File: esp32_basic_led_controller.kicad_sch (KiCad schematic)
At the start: 16 parts, among them J1 Barrel_Jack_Switch_Pin3Ring, J2 Conn_01x03, J3 Screw_Terminal_01x02, Q1 IRF8721PBF-1, SW1 SW_DIP_x01, U1 ESP32-WROOM-32U, U2 LD1117S33TR_SOT223, U3 I2C_SENS_1

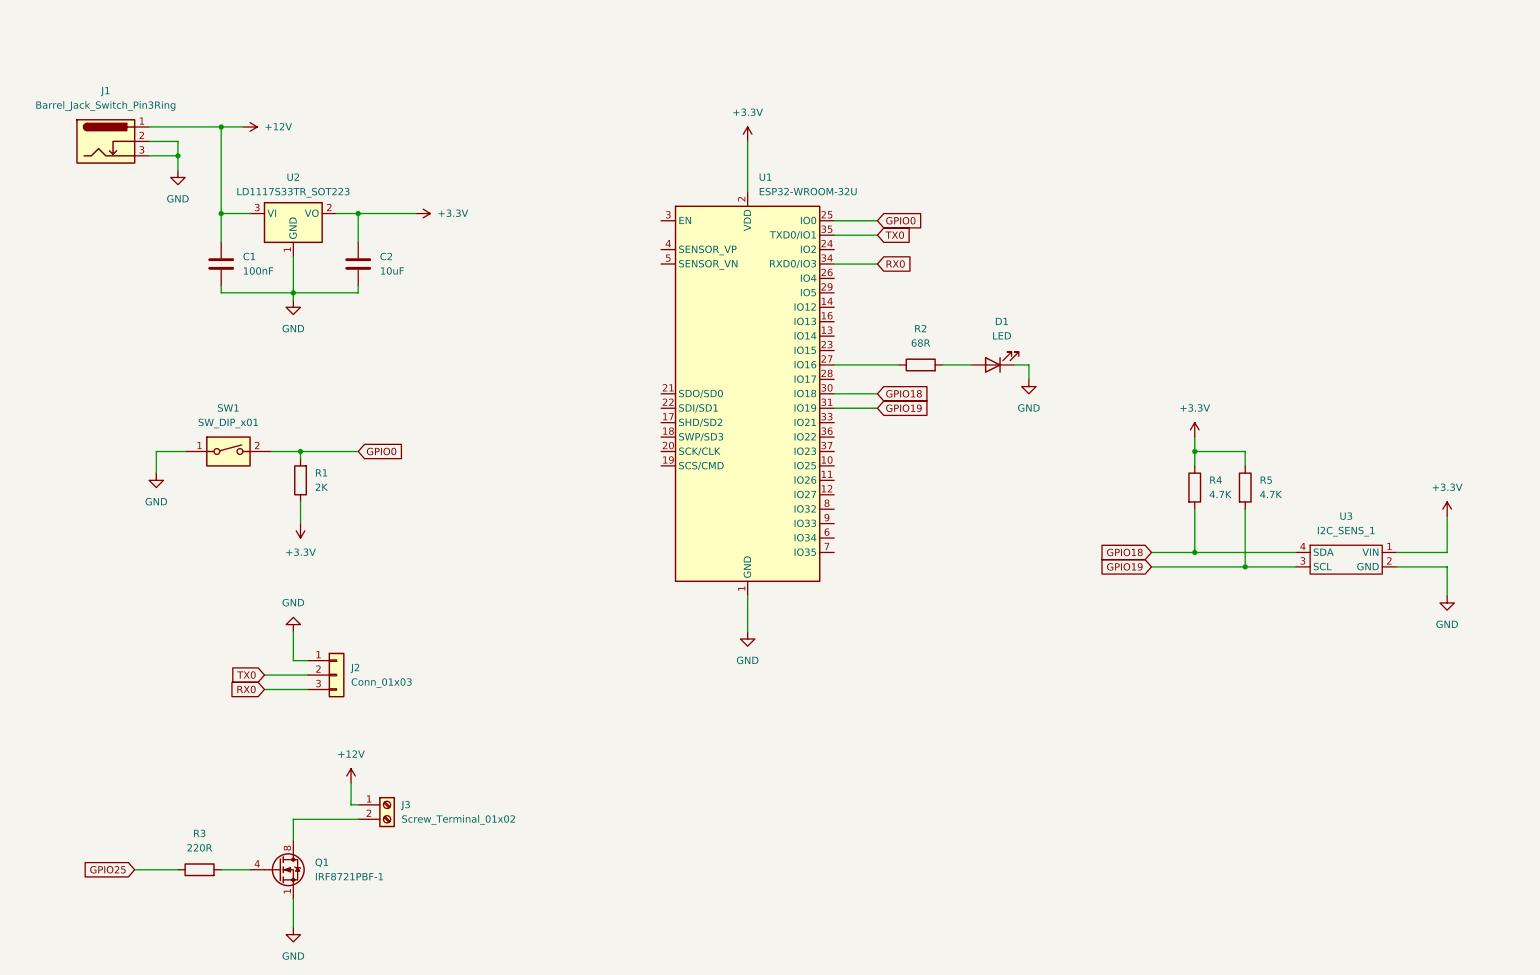
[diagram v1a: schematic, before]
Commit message: Migrated to ESP32-C3-Mini-1 SoC
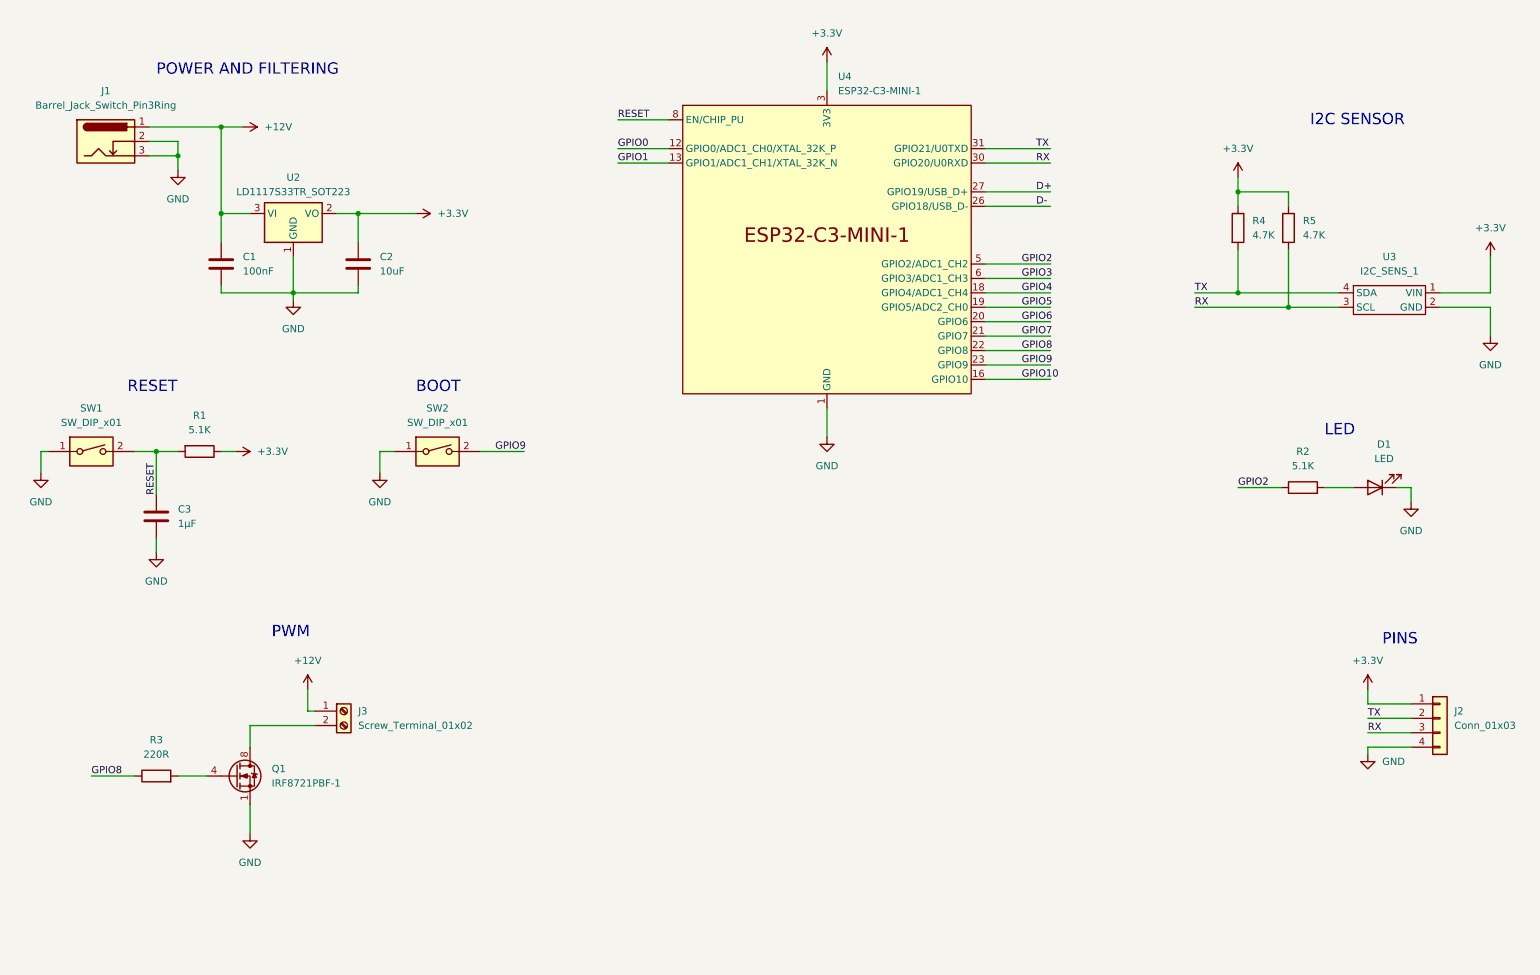
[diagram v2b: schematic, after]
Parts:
- removed U1: ESP32-WROOM-32U, RF_Module:ESP32-WROOM-32U, symbol RF_Module:ESP32-WROOM-32U
- added C3: 1μF, symbol Device:C
- added SW2: SW_DIP_x01, symbol Switch:SW_DIP_x01
- added U4: ESP32-C3-MINI-1, Espressif:ESP32-C3-MINI-1, symbol PCM_Espressif:ESP32-C3-MINI-1
- J2: symbol Connector_Generic:Conn_01x03 -> Connector_Generic:Conn_01x04
- R1: value 2K -> 5.1K
- R2: value 68R -> 5.1K
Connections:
- net RX0 is gone; now on net RX: J2.3 (Pin_3)
- net TX0 is gone; now on net TX: J2.2 (Pin_2)
- net +3.3V: now also J2.1 (Pin_1), U4.3 (3V3)
- net GND: now also J2.4 (Pin_4), C3.2, SW2.1, U4.1 (GND), U4.11 (GND), U4.14 (GND), U4.2 (GND), U4.36 (GND), U4.37 (GND), U4.38 (GND), U4.39 (GND), U4.40 (GND), U4.41 (GND), U4.42 (GND), U4.43 (GND), U4.44 (GND), U4.45 (GND), U4.46 (GND), U4.47 (GND), U4.48 (GND), U4.49 (GND), U4.50 (GND), U4.51 (GND), U4.52 (GND), U4.53 (GND); no longer J2.1 (Pin_1)
- net GPIO0: now also U4.12 (GPIO0/ADC1_CH0/XTAL_32K_P); no longer R1.2, SW1.2
- net GPIO2: now reaches R2.1
- net GPIO2: now also U4.5 (GPIO2/ADC1_CH2)
- net GPIO18 renamed TX
- net TX: now also U4.31 (GPIO21/U0TXD)
- net GPIO19 renamed RX
- net RX: now also U4.30 (GPIO20/U0RXD)
- net GPIO25 renamed GPIO8
- net GPIO8: now also U4.22 (GPIO8)
- new net D+: U4.27 (GPIO19/USB_D+)
- new net D-: U4.26 (GPIO18/USB_D-)
- new net GPIO1: U4.13 (GPIO1/ADC1_CH1/XTAL_32K_N)
- new net GPIO10: U4.16 (GPIO10)
- new net GPIO3: U4.6 (GPIO3/ADC1_CH3)
- new net GPIO4: U4.18 (GPIO4/ADC1_CH4)
- new net GPIO5: U4.19 (GPIO5/ADC2_CH0)
- new net GPIO6: U4.20 (GPIO6)
- new net GPIO7: U4.21 (GPIO7)
- new net GPIO9: SW2.2, U4.23 (GPIO9)
- new net RESET: C3.1, R1.2, SW1.2, U4.8 (EN/CHIP_PU)
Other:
- note added: "BOOT"
- note added: "I2C SENSOR"
- note added: "LED"
- note added: "PINS"
- note added: "POWER AND FILTERING"
- note added: "PWM"
- note added: "RESET"
- moved on the sheet: D1, J3, Q1, R1, R2, R3, R4, R5, SW1, U3

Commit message: Vertical board layout
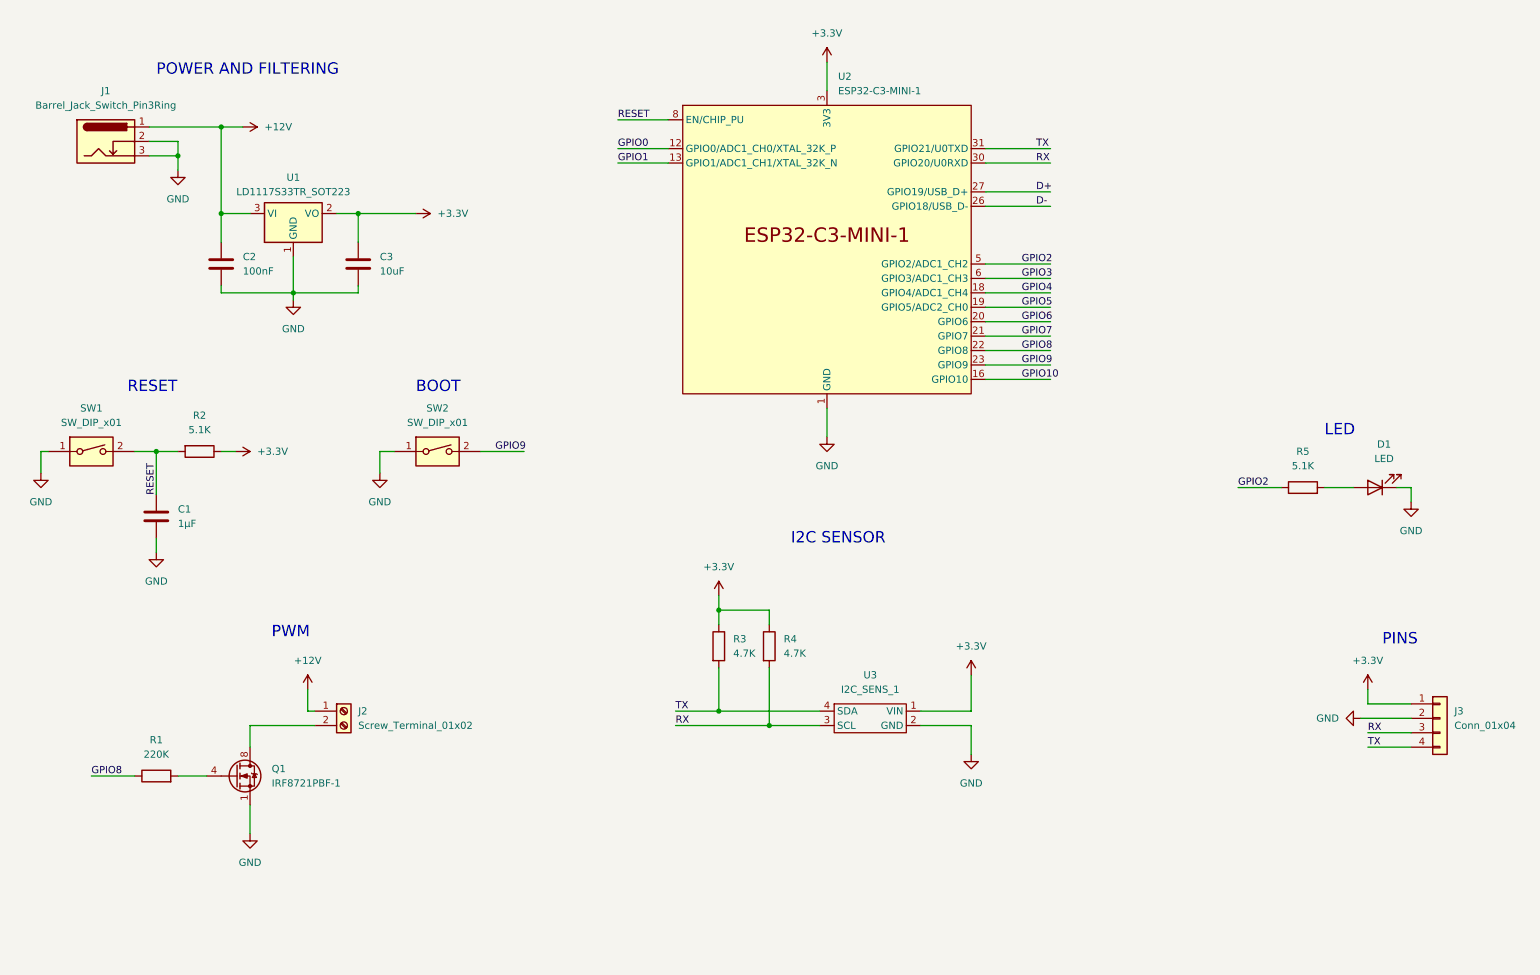
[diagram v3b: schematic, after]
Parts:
- C1: renamed from C3; footprint (none) -> Capacitor_SMD:C_0603_1608Metric_Pad1.08x0.95mm_HandSolder
- J3: renamed from J2; value Conn_01x03 -> Conn_01x04; footprint Connector_PinHeader_1.27mm:PinHeader_1x03_P1.27mm_Vertical -> Connector_PinHeader_1.27mm:PinHeader_1x04_P1.27mm_Vertical
- R1: renamed from R3; value 220R -> 220K
- SW2: footprint (none) -> Button_Switch_SMD:SW_Push_1P1T_NO_6x6mm_H9.5mm
- U2: renamed from U4; footprint Espressif:ESP32-C3-MINI-1 -> PCM_Espressif:ESP32-C3-MINI-1
- renumbered C1 to C2, C2 to C3, J3 to J2, R1 to R2, R4 to R3, R5 to R4, R2 to R5, U2 to U1
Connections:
- net GND: now also J3.2 (Pin_2); no longer J3.4 (Pin_4)
- net TX: now also J3.4 (Pin_4); no longer J3.2 (Pin_2)
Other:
- moved on the sheet: R3, R4, U3

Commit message: Board layout tweaks
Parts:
- added H1, H2, H3, H4: MountingHole, MountingHole:MountingHole_2.2mm_M2_DIN965, symbol Mechanical:MountingHole
- D1: footprint LED_SMD:LED_1206_3216Metric_Pad1.42x1.75mm_HandSolder -> LED_SMD:LED_0603_1608Metric_Pad1.05x0.95mm_HandSolder
- R2: footprint Resistor_SMD:R_0201_0603Metric_Pad0.64x0.40mm_HandSolder -> Resistor_SMD:R_0603_1608Metric_Pad0.98x0.95mm_HandSolder
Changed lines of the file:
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@@
   (junction (at 147.32 144.78) (diameter 0) (color 0 0 0 0)
   )
+  (junction (at 157.48 92.71) (diameter 0) (color 0 0 0 0)
+  )
   (junction (at 50.8 54.61) (diameter 0) (color 0 0 0 0)
   )
@@
     (stroke (width 0) (type default))
   )
-  (wire (pts (xy 157.48 88.9) (xy 157.48 93.98))
+  (wire (pts (xy 157.48 88.9) (xy 157.48 92.71))
     (stroke (width 0) (type default))
   )
@@
     (stroke (width 0) (type default))
   )
+  (wire (pts (xy 157.48 92.71) (xy 161.29 92.71))
+    (stroke (width 0) (type default))
+  )
   (wire (pts (xy 185.42 53.34) (xy 196.85 53.34))
     (stroke (width 0) (type default))
@@
     (stroke (width 0) (type default))
   )
+  (wire (pts (xy 157.48 92.71) (xy 157.48 93.98))
+    (stroke (width 0) (type default))
+  )
   (wire (pts (xy 96.52 96.52) (xy 104.14 96.52))
     (stroke (width 0) (type default))
@@
   )
   (wire (pts (xy 260.35 102.87) (xy 260.35 105.41))
+    (stroke (width 0) (type default))
+  )
+  (wire (pts (xy 50.8 34.29) (xy 50.8 39.37))
     (stroke (width 0) (type default))
   )
@@
     (effects (font (size 2 2)) (justify left bottom))
   )
-  (text "POWER AND FILTERING" (at 39.37 30.48 0)
+  (text "POWER AND FILTERING" (at 34.29 26.67 0)
     (effects (font (size 2 2)) (justify left bottom))
   )
@@
     )
   )
+  (symbol (lib_id "Mechanical:MountingHole") (at 254 40.64 0) (unit 1)
+    (in_bom yes) (on_board yes) (dnp no) (fields_autoplaced)
+    (property "Reference" "H4" (at 256.54 39.37 0)
+      (effects (font (size 1.27 1.27)) (justify left))
+    )
+    (property "Value" "MountingHole" (at 256.54 41.91 0)
+      (effects (font (size 1.27 1.27)) (justify left))
+    )
+    (property "Footprint" "MountingHole:MountingHole_2.2mm_M2_DIN965" (at 254 40.64 0)
+      (effects (font (size 1.27 1.27)) hide)
+    )
+    (property "Datasheet" "~" (at 254 40.64 0)
+      (effects (font (size 1.27 1.27)) hide)
+    )
+    (instances
+      (project "esp32_basic_led_controller"
+        (path "/32e7cfc9-9723-4338-afdf-87df69ece0a8"
+          (reference "H4") (unit 1)
+        )
+      )
+    )
+  )
   (symbol (lib_id "power:GND") (at 157.48 93.98 0) (unit 1)
     (in_bom yes) (on_board yes) (dnp no) (fields_autoplaced)
@@
       (effects (font (size 1.27 1.27)))
     )
-    (property "Footprint" "LED_SMD:LED_1206_3216Metric_Pad1.42x1.75mm_HandSolder" (at 254 102.87 0)
+    (property "Footprint" "LED_SMD:LED_0603_1608Metric_Pad1.05x0.95mm_HandSolder" (at 254 102.87 0)
       (effects (font (size 1.27 1.27)) hide)
     )
@@
       (effects (font (size 1.27 1.27)))
     )
-    (property "Footprint" "Resistor_SMD:R_0201_0603Metric_Pad0.64x0.40mm_HandSolder" (at 46.99 94.742 90)
+    (property "Footprint" "Resistor_SMD:R_0603_1608Metric_Pad0.98x0.95mm_HandSolder" (at 46.99 94.742 90)
       (effects (font (size 1.27 1.27)) hide)
     )
@@
     )
   )
+  (symbol (lib_id "power:PWR_FLAG") (at 50.8 34.29 0) (unit 1)
+    (in_bom yes) (on_board yes) (dnp no) (fields_autoplaced)
+    (property "Reference" "#FLG01" (at 50.8 32.385 0)
+      (effects (font (size 1.27 1.27)) hide)
+    )
+    (property "Value" "PWR_FLAG" (at 50.8 29.21 0)
+      (effects (font (size 1.27 1.27)))
+    )
+    (property "Footprint" "" (at 50.8 34.29 0)
+      (effects (font (size 1.27 1.27)) hide)
+    )
+    (property "Datasheet" "~" (at 50.8 34.29 0)
+      (effects (font (size 1.27 1.27)) hide)
+    )
+    (pin "1")
+    (instances
+      (project "esp32_basic_led_controller"
+        (path "/32e7cfc9-9723-4338-afdf-87df69ece0a8"
+          (reference "#FLG01") (unit 1)
+        )
+      )
+    )
+  )
+  (symbol (lib_id "power:PWR_FLAG") (at 161.29 92.71 270) (unit 1)
+    (in_bom yes) (on_board yes) (dnp no) (fields_autoplaced)
+    (property "Reference" "#FLG02" (at 163.195 92.71 0)
+      (effects (font (size 1.27 1.27)) hide)
+    )
+    (property "Value" "PWR_FLAG" (at 165.1 92.71 90)
+      (effects (font (size 1.27 1.27)) (justify left))
+    )
+    (property "Footprint" "" (at 161.29 92.71 0)
+      (effects (font (size 1.27 1.27)) hide)
+    )
+    (property "Datasheet" "~" (at 161.29 92.71 0)
+      (effects (font (size 1.27 1.27)) hide)
+    )
+    (pin "1")
+    (instances
+      (project "esp32_basic_led_controller"
+        (path "/32e7cfc9-9723-4338-afdf-87df69ece0a8"
+          (reference "#FLG02") (unit 1)
+        )
+      )
+    )
+  )
   (symbol (lib_id "Device:R") (at 138.43 130.81 0) (unit 1)
     (in_bom yes) (on_board yes) (dnp no) (fields_autoplaced)
@@
     )
   )
+  (symbol (lib_id "Mechanical:MountingHole") (at 254 27.94 0) (unit 1)
+    (in_bom yes) (on_board yes) (dnp no) (fields_autoplaced)
+    (property "Reference" "H2" (at 256.54 26.67 0)
+      (effects (font (size 1.27 1.27)) (justify left))
+    )
+    (property "Value" "MountingHole" (at 256.54 29.21 0)
+      (effects (font (size 1.27 1.27)) (justify left))
+    )
+    (property "Footprint" "MountingHole:MountingHole_2.2mm_M2_DIN965" (at 254 27.94 0)
+      (effects (font (size 1.27 1.27)) hide)
+    )
+    (property "Datasheet" "~" (at 254 27.94 0)
+      (effects (font (size 1.27 1.27)) hide)
+    )
+    (instances
+      (project "esp32_basic_led_controller"
+        (path "/32e7cfc9-9723-4338-afdf-87df69ece0a8"
+          (reference "H2") (unit 1)
+        )
+      )
+    )
+  )
   (symbol (lib_id "power:GND") (at 260.35 105.41 0) (unit 1)
     (in_bom yes) (on_board yes) (dnp no) (fields_autoplaced)
@@
         (path "/32e7cfc9-9723-4338-afdf-87df69ece0a8"
           (reference "SW1") (unit 1)
+        )
+      )
+    )
+  )
+  (symbol (lib_id "Mechanical:MountingHole") (at 254 34.29 0) (unit 1)
+    (in_bom yes) (on_board yes) (dnp no) (fields_autoplaced)
+    (property "Reference" "H3" (at 256.54 33.02 0)
+      (effects (font (size 1.27 1.27)) (justify left))
+    )
+    (property "Value" "MountingHole" (at 256.54 35.56 0)
+      (effects (font (size 1.27 1.27)) (justify left))
+    )
+    (property "Footprint" "MountingHole:MountingHole_2.2mm_M2_DIN965" (at 254 34.29 0)
+      (effects (font (size 1.27 1.27)) hide)
+    )
+    (property "Datasheet" "~" (at 254 34.29 0)
+      (effects (font (size 1.27 1.27)) hide)
+    )
+    (instances
+      (project "esp32_basic_led_controller"
+        (path "/32e7cfc9-9723-4338-afdf-87df69ece0a8"
+          (reference "H3") (unit 1)
         )
       )
@@
         )
       )
+    )
+  )
+  (symbol (lib_id "Mechanical:MountingHole") (at 254 21.59 0) (unit 1)
+    (in_bom yes) (on_board yes) (dnp no) (fields_autoplaced)
+    (property "Reference" "H1" (at 256.54 20.32 0)
+      (effects (font (size 1.27 1.27)) (justify left))
+    )
+    (property "Value" "MountingHole" (at 256.54 22.86 0)
+      (effects (font (size 1.27 1.27)) (justify left))
+    )
+    (property "Footprint" "MountingHole:MountingHole_2.2mm_M2_DIN965" (at 254 21.59 0)
+      (effects (font (size 1.27 1.27)) hide)
+    )
+    (property "Datasheet" "~" (at 254 21.59 0)
+      (effects (font (size 1.27 1.27)) hide)
+    )
+    (instances
+      (project "esp32_basic_led_controller"
+        (path "/32e7cfc9-9723-4338-afdf-87df69ece0a8"
+          (reference "H1") (unit 1)
+        )
+      )

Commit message: Finished PCB routing and layout
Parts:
- SW1, SW2: value SW_DIP_x01 -> TSA343G00-250J2; footprint Button_Switch_SMD:SW_Push_1P1T_NO_6x6mm_H9.5mm -> User:TSA343G00-250J2; symbol Switch:SW_DIP_x01 -> Switch:SW_SPST
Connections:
- net GPIO1: now also R5.1
- net GPIO2: no longer R5.1
- no-connect marks 0 -> 10
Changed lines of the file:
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@@
   (junction (at 50.8 39.37) (diameter 0) (color 0 0 0 0)
   )
+  (no_connect (at 196.85 71.12))
+  (no_connect (at 196.85 50.8))
+  (no_connect (at 196.85 68.58))
+  (no_connect (at 196.85 53.34))
+  (no_connect (at 196.85 66.04))
+  (no_connect (at 196.85 76.2))
+  (no_connect (at 196.85 63.5))
+  (no_connect (at 120.65 43.18))
+  (no_connect (at 196.85 73.66))
+  (no_connect (at 196.85 83.82))
   (wire (pts (xy 39.37 111.76) (xy 39.37 114.3))
     (stroke (width 0) (type default))
@@
     (stroke (width 0) (type default))
   )
-  (wire (pts (xy 81.28 96.52) (xy 78.74 96.52))
-    (stroke (width 0) (type default))
-  )
-  (wire (pts (xy 35.56 96.52) (xy 39.37 96.52))
+  (wire (pts (xy 78.74 96.52) (xy 83.82 96.52))
+    (stroke (width 0) (type default))
+  )
+  (wire (pts (xy 33.02 96.52) (xy 39.37 96.52))
     (stroke (width 0) (type default))
   )
@@
     (stroke (width 0) (type default))
   )
-  (wire (pts (xy 96.52 96.52) (xy 104.14 96.52))
+  (wire (pts (xy 93.98 96.52) (xy 104.14 96.52))
     (stroke (width 0) (type default))
   )
@@
     (stroke (width 0) (type default))
   )
-  (wire (pts (xy 19.05 96.52) (xy 20.32 96.52))
+  (wire (pts (xy 19.05 96.52) (xy 22.86 96.52))
     (stroke (width 0) (type default))
   )
@@
     (effects (font (size 1.27 1.27)) (justify left bottom))
   )
-  (label "GPIO2" (at 229.87 102.87 0) (fields_autoplaced)
+  (label "GPIO1" (at 229.87 102.87 0) (fields_autoplaced)
     (effects (font (size 1.27 1.27)) (justify left bottom))
   )
@@
     )
   )
-  (symbol (lib_id "Switch:SW_DIP_x01") (at 88.9 96.52 0) (unit 1)
+  (symbol (lib_id "Switch:SW_SPST") (at 88.9 96.52 0) (unit 1)
     (in_bom yes) (on_board yes) (dnp no) (fields_autoplaced)
     (property "Reference" "SW2" (at 88.9 88.9 0)
       (effects (font (size 1.27 1.27)))
     )
-    (property "Value" "SW_DIP_x01" (at 88.9 91.44 0)
-      (effects (font (size 1.27 1.27)))
-    )
-    (property "Footprint" "Button_Switch_SMD:SW_Push_1P1T_NO_6x6mm_H9.5mm" (at 88.9 96.52 0)
+    (property "Value" "TSA343G00-250J2" (at 88.9 91.44 0)
+      (effects (font (size 1.27 1.27)))
+    )
+    (property "Footprint" "User:TSA343G00-250J2" (at 88.9 96.52 0)
       (effects (font (size 1.27 1.27)) hide)
     )
@@
     )
   )
-  (symbol (lib_id "Switch:SW_DIP_x01") (at 27.94 96.52 0) (unit 1)
+  (symbol (lib_id "Switch:SW_SPST") (at 27.94 96.52 0) (unit 1)
     (in_bom yes) (on_board yes) (dnp no) (fields_autoplaced)
     (property "Reference" "SW1" (at 27.94 88.9 0)
       (effects (font (size 1.27 1.27)))
     )
-    (property "Value" "SW_DIP_x01" (at 27.94 91.44 0)
-      (effects (font (size 1.27 1.27)))
-    )
-    (property "Footprint" "Button_Switch_SMD:SW_Push_1P1T_NO_6x6mm_H9.5mm" (at 27.94 96.52 0)
-      (effects (font (size 1.27 1.27)) hide)
-    )
+    (property "Value" "TSA343G00-250J2" (at 27.94 91.44 0)
+      (effects (font (size 1.27 1.27)))
+    )
+    (property "Footprint" "User:TSA343G00-250J2" (at 27.94 96.52 0)
+      (effects (font (size 1.27 1.27)) hide)
+    )
